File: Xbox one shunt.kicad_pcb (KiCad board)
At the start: 2 copper layers, 13.5 x 14.2 mm, 13 parts, among them U1 INA181A1-Q1, U2 TLV3201AIDCKR

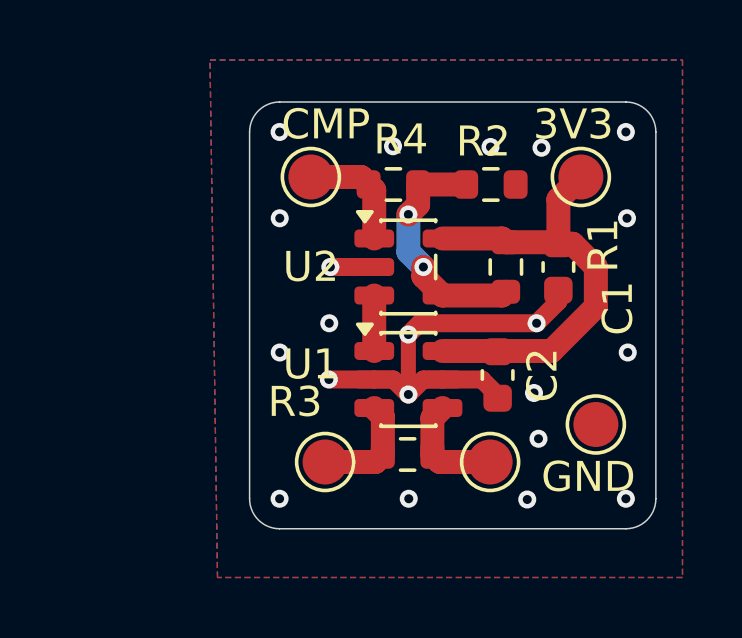
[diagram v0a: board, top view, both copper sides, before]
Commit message: added a U.FL SMT conector for an osciloscope
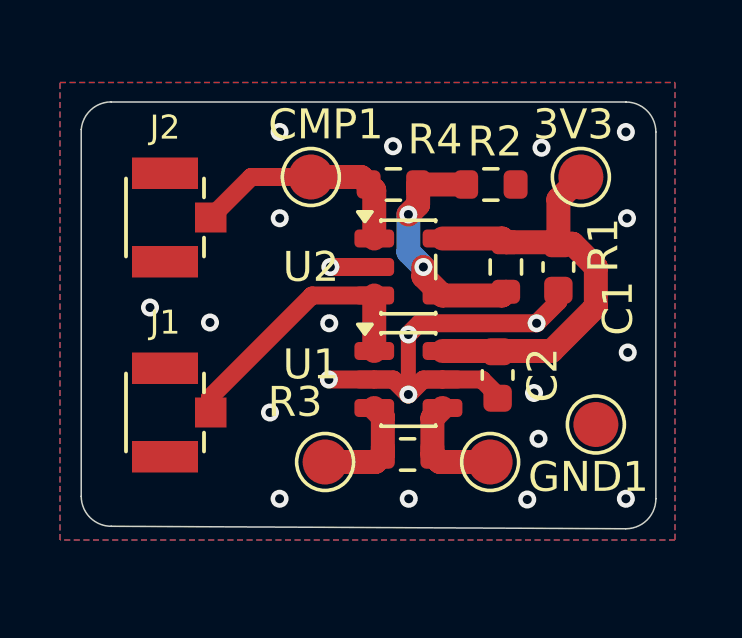
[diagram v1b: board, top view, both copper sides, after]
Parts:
- added J1: U.FL-R-SMT-1_10_, U.FL-R-SMT-1_10:HRS_U.FL-R-SMT-1_10_, F.Cu at (85.5, 105.0)
- added J2: U.FL-R-SMT-1_10_, U.FL-R-SMT-1_10:HRS_U.FL-R-SMT-1_10_, F.Cu at (85.5, 98.5)
- renumbered CMP to CMP1, GND to GND1
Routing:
- net /AMP_OUT: track 1.85 -> 9.26 mm
- net /CMP_OUT: track 4.16 -> 8.05 mm
- net GND: vias 21 -> 22
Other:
- board size 13.5 x 14.2 mm -> 19.2 x 14.2 mm

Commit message: pcb and sch fixes
Replaced TLV3201AIDCKR (SC70-5) which was using an SOT-23-5 footprint with a TLV3201AIDBVR (same specs and correct footprint)
Updated schematic and PCB for above change
Added Libraries directory and applied to project
Edited symbols
Fixed silks
Added 3D models
Some general cleaning in schematic and PCB
Clean DRC
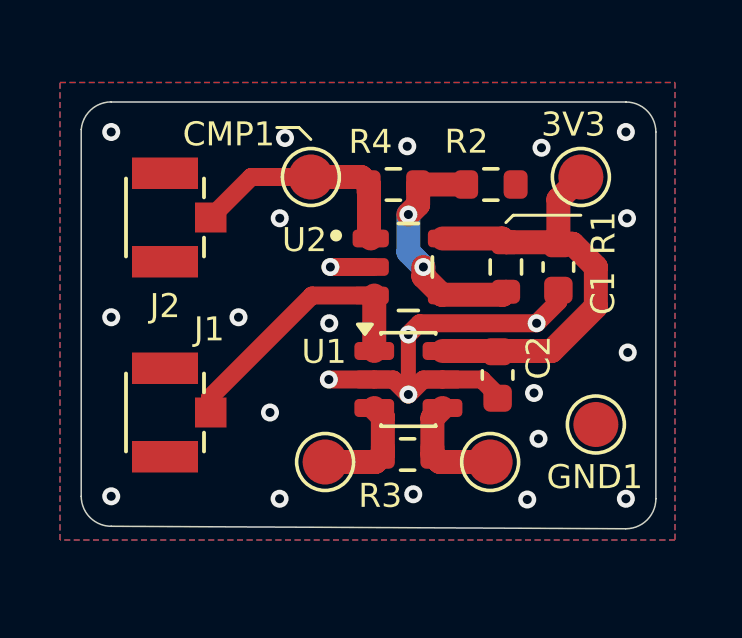
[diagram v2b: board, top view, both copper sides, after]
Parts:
- J1, J2: footprint U.FL-R-SMT-1_10:HRS_U.FL-R-SMT-1_10_ -> U.FL-R-SMT-1_10_:HRS_U.FL-R-SMT-1_10_
- U2: value TLV3201AIDCKR -> TLV3201AIDBVR; footprint Package_TO_SOT_SMD:SOT-23-5 -> TLV3201AIDBVR:TLV3201AIDBVR
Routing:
- net GND: vias 22 -> 24
